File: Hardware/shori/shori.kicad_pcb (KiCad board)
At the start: 4 copper layers, 102.8 x 41 mm, 114 parts, among them U1 CS4272, U2 STM32H750VBTx, U3 NE5532, U4 NE5532, U5 TPS73733DCQR, U6 W25Q128JVS, U7 TLV9001IDCK, Y1 16MHz

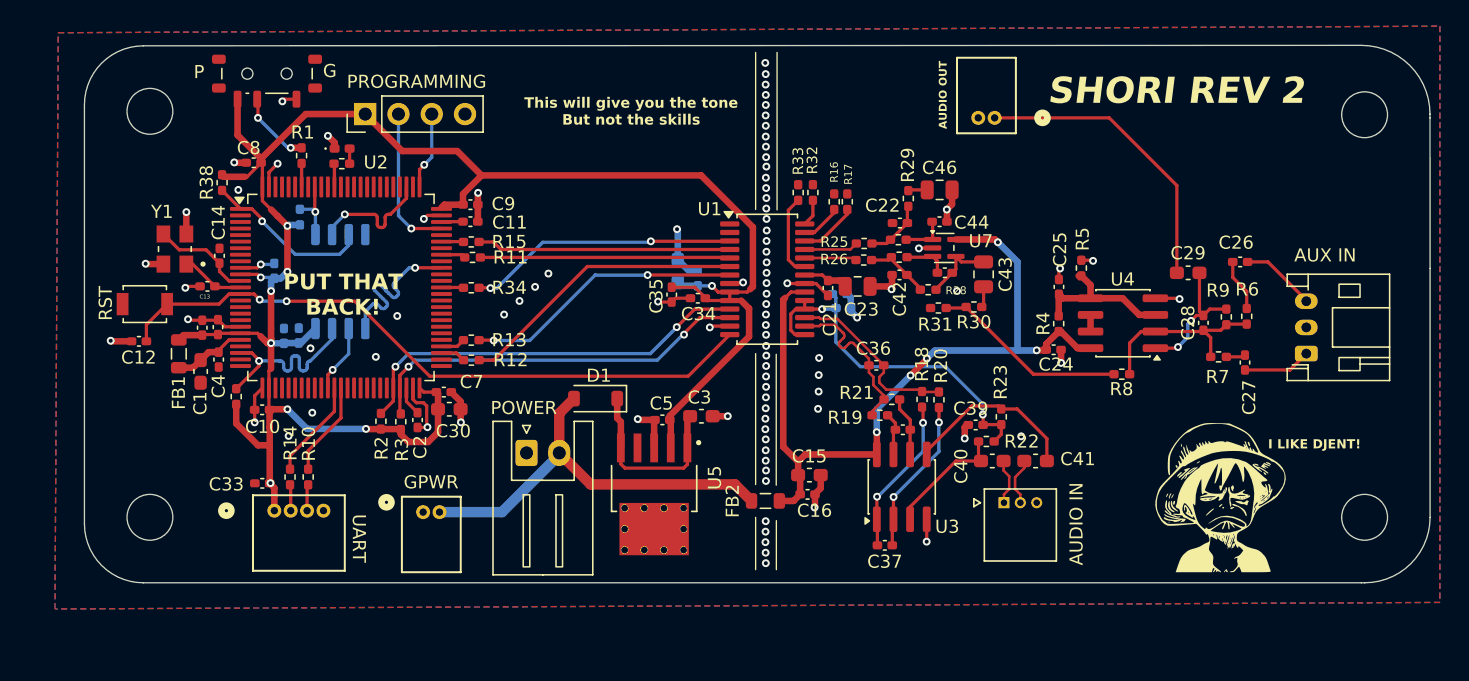
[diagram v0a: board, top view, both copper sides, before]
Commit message: Rev 3 changes: RC filters, Ideal diodes, electrical fixes, and their layout
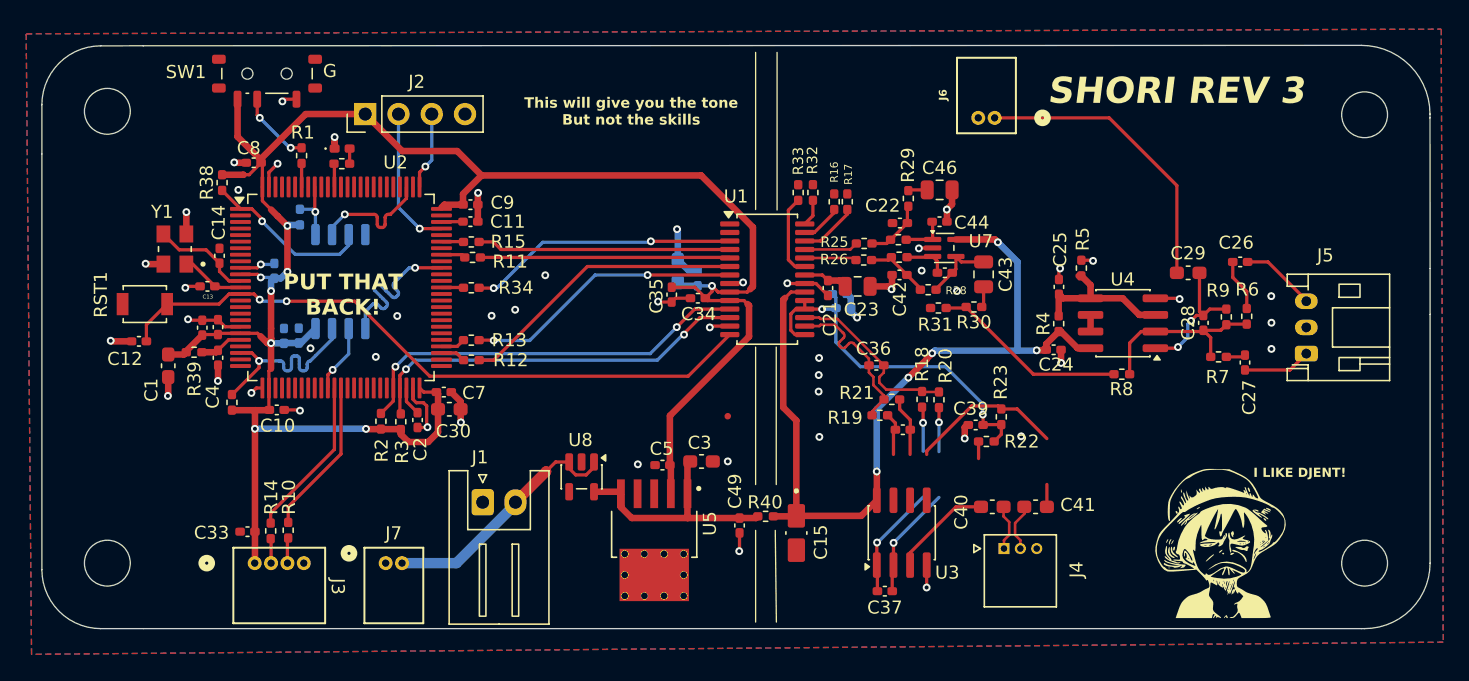
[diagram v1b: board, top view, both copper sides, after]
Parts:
- removed C16: 100nF, Capacitor_SMD:C_0402_1005Metric_Pad0.74x0.62mm_HandSolder
- removed D1: D_Schottky, Diode_SMD:D_SOD-123
- removed FB1, FB2: FerriteBead, Inductor_SMD:L_0805_2012Metric
- added C49: 100nF, Capacitor_SMD:C_0402_1005Metric_Pad0.74x0.62mm_HandSolder, F.Cu at (150.3, 127.6)
- added R39: 10Ω, Resistor_SMD:R_0402_1005Metric_Pad0.72x0.64mm_HandSolder, F.Cu at (108.6, 114.4)
- added R40: 10Ω, Resistor_SMD:R_0402_1005Metric_Pad0.72x0.64mm_HandSolder, F.Cu at (152.3, 126.9)
- added U8: MAX40200AUK, Package_TO_SOT_SMD:SOT-23-5, F.Cu at (138.2, 123.9)
- C1: value 4.7uf -> 100nF
- C15: value 10μF -> 100uF; footprint Capacitor_SMD:C_0603_1608Metric_Pad1.08x0.95mm_HandSolder -> MyFootprints:CAPPM3216X180N
- C4: value 100nF -> 10uF
- J4: renamed from AUDIO IN
- J5: renamed from AUX IN
- J6: renamed from AUDIO OUT
- moved J1 5.04 mm to (130.7, 125.8)
- moved J7 4.83 mm to (123.2, 130.5)
- moved H3 4.78 mm to (102.0, 130.5)
- moved C15 4.53 mm to (154.6, 128.2), turned to -90 degrees
- moved R14 4.37 mm to (114.5, 128.0)
- moved R10 4.34 mm to (115.8, 128.0)
- moved J3 4.28 mm to (113.2, 130.5)
- moved C33 3.86 mm to (112.7, 128.1)
- moved U5 3.50 mm to (143.8, 128.3)
- moved J4 3.50 mm to (170.5, 129.4)
- moved U3 3.50 mm to (162.7, 128.2)
- moved C37 3.50 mm to (161.4, 132.6)
- moved C40 3.50 mm to (169.6, 126.2)
- moved C41 3.50 mm to (172.9, 126.2)
- moved G*** 3.50 mm to (187.4, 127.5)
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- renumbered POWER to J1, PROGRAMMING to J2, UART to J3, GPWR to J7, RST to RST1, P to SW1
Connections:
- net Net-(D1-K) renamed /5V_PROTECTED
- C1 pad 1: +3.3VA -> +3.3V
- J2 pad 2: /SWCLK -> /SWDIO
- J2 pad 3: /SWDIO -> /SWCLK
- U2 pad 72: /SWCLK -> /SWDIO
- U2 pad 76: /SWDIO -> /SWCLK
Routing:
- net +5V: track 31.9 -> 19.4 mm
- net +3.3V: track 154.7 -> 162.9 mm, vias 9 -> 8
- net /5V_PROTECTED: track 14.2 -> 20.0 mm
- net GND: track 67.8 -> 62.3 mm, vias 95 -> 52
- net /SWCLK: track 11.4 -> 5.95 mm
- net +5VA: track 60.5 -> 65.9 mm
- net /SWDIO: track 5.95 -> 11.1 mm
- net /UART_RX_RES: track 7.60 -> 12.3 mm
- net /UART_TX_RES: track 7.24 -> 11.9 mm
- net +3.3VA: track 5.67 -> 3.34 mm
- net /QSPI_IO3: track 15.4 -> 16.0 mm
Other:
- board size 102.8 x 41 mm -> 106 x 44.5 mm
- board text added: "SHORI REV 3"
- board text removed: "SHORI REV 2"

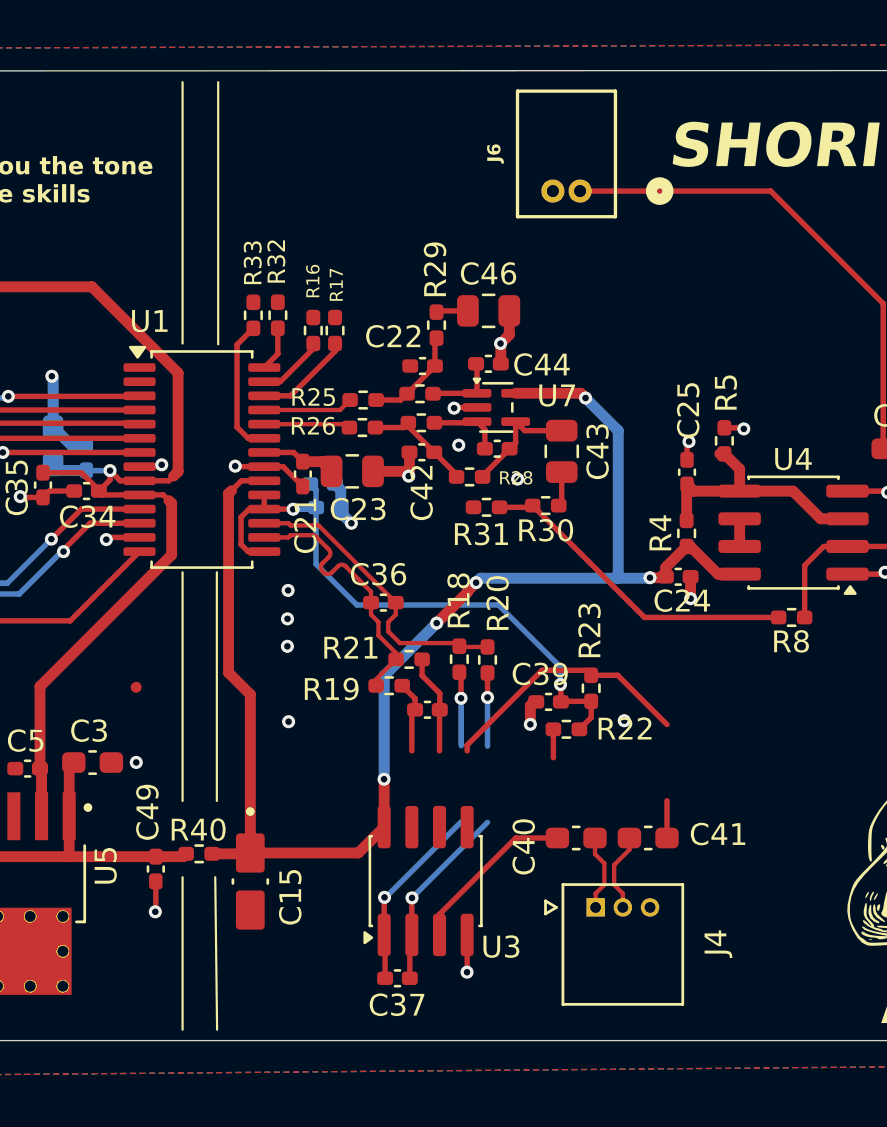
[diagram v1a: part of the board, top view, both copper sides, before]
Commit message: Power LED added on schems
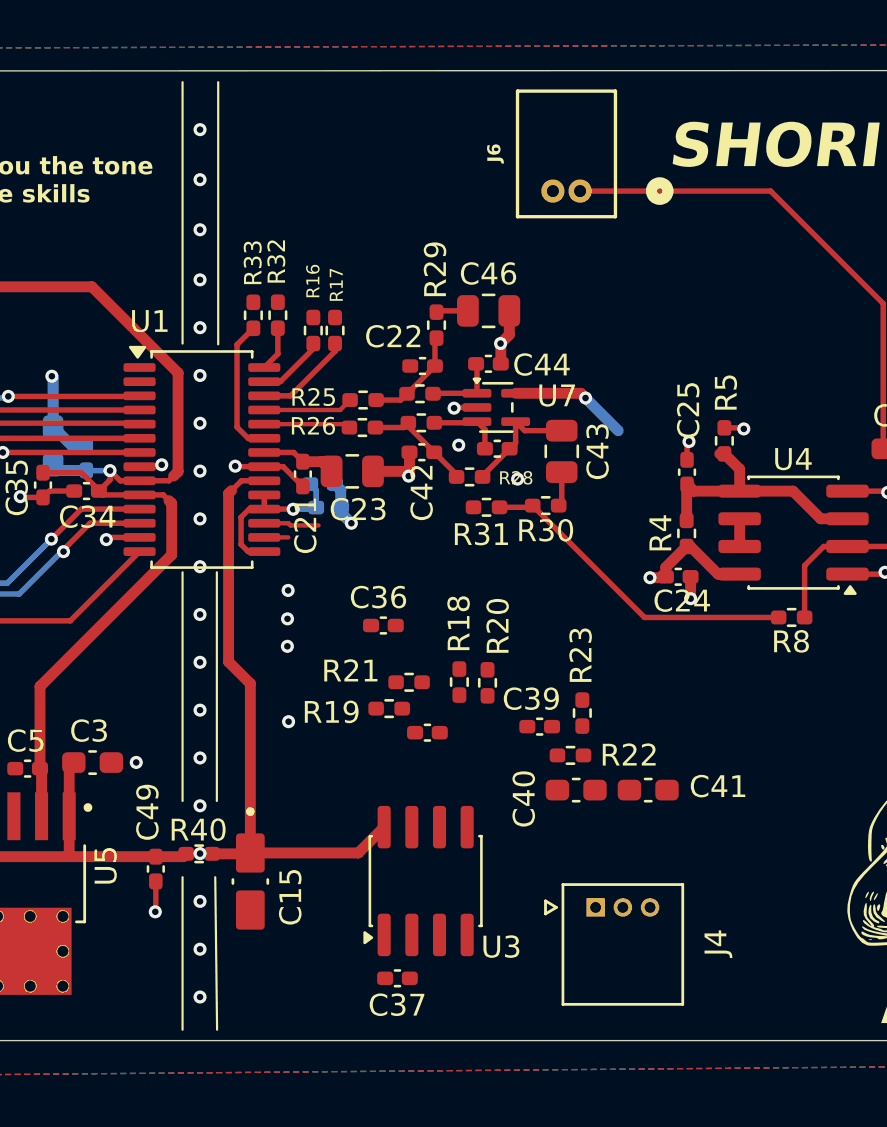
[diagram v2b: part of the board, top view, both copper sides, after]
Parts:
- moved C40 2.20 mm to (169.6, 124.0)
- moved C41 2.20 mm to (172.9, 124.0)
- moved R22 1.21 mm to (169.3, 122.4)
- moved C39 1.21 mm to (167.9, 121.1)
- moved R23 1.21 mm to (169.9, 120.5)
- moved R18 1.05 mm to (164.2, 119.0)
- moved R20 1.05 mm to (165.5, 119.1)
- moved C36 1.05 mm to (160.7, 116.4)
- moved C38 1.05 mm to (162.7, 121.4)
- moved R19 1.05 mm to (161.0, 120.3)
- moved R21 1.05 mm to (161.9, 119.0)
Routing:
- net +5VA: track 65.9 -> 38.1 mm, vias 5 -> 2
- net /VCOM: track 28.2 -> 7.92 mm, vias 2 -> 1
- net Net-(U3B-+): track 13.6 -> 0.00 mm
- net Net-(C37-Pad1): track 12.1 -> 0.00 mm, vias 2 -> 0
- net Net-(U3A--): track 12.0 -> 0.00 mm, vias 2 -> 0
- net /CODEC_AIN-: track 12.5 -> 1.11 mm
- net /CODEC_AIN+: track 13.9 -> 2.53 mm
- net Net-(U3A-+): track 9.38 -> 0.00 mm
- net Net-(U3B--): track 4.54 -> 0.00 mm
- net /AUDIO_IN-: track 3.64 -> 0.00 mm
- net /AUDIO_IN+: track 3.53 -> 0.00 mm
- net Net-(C38-Pad1): track 3.30 -> 0.00 mm
- net GND: track 62.3 -> 59.4 mm, vias 52 -> 68

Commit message: Rev 3 main changes completed!
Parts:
- added D1: LED, LED_SMD:LED_0603_1608Metric_Pad1.05x0.95mm_HandSolder, F.Cu at (138.7, 119.5)
- added D10: BAT54C, Package_TO_SOT_SMD:SOT-23, F.Cu at (188.9, 106.7)
- added D11: BAT54C, Package_TO_SOT_SMD:SOT-23, F.Cu at (189.4, 118.9)
- added D7: PRTR5V0U2X, Package_TO_SOT_SMD:SOT-143, F.Cu at (121.5, 124.4)
- added D8: BAT54C, Package_TO_SOT_SMD:SOT-23, F.Cu at (166.5, 127.3)
- added D9: BAT54C, Package_TO_SOT_SMD:SOT-23, F.Cu at (175.8, 126.5)
- added R41: 33Ω, Resistor_SMD:R_0402_1005Metric_Pad0.72x0.64mm_HandSolder, F.Cu at (142.4, 119.5)
- added R42: 100Ω, Resistor_SMD:R_0402_1005Metric_Pad0.72x0.64mm_HandSolder, F.Cu at (172.5, 126.4)
- added R43: 100Ω, Resistor_SMD:R_0402_1005Metric_Pad0.72x0.64mm_HandSolder, F.Cu at (169.9, 126.4)
- added R44: 100Ω, Resistor_SMD:R_0402_1005Metric_Pad0.72x0.64mm_HandSolder, F.Cu at (191.7, 106.8)
- added R45: 100Ω, Resistor_SMD:R_0402_1005Metric_Pad0.72x0.64mm_HandSolder, F.Cu at (192.3, 118.3)
- added TP1: TP_5V, TestPoint:TestPoint_Pad_D1.0mm, F.Cu at (149.0, 127.1)
- added TP2: TP_3V3, TestPoint:TestPoint_Pad_D1.0mm, F.Cu at (145.0, 119.5)
- added TP3: TP_3V3A, TestPoint:TestPoint_Pad_D1.0mm, F.Cu at (106.0, 116.5)
- added TP4: TP_5VA, TestPoint:TestPoint_Pad_D1.0mm, F.Cu at (156.0, 120.5)
- added TP5: TP_MCLK, TestPoint:TestPoint_Pad_D1.0mm, B.Cu at (138.0, 106.0)
- added TP6: TP_UARTTX, TestPoint:TestPoint_Pad_D1.0mm, F.Cu at (118.0, 124.0)
- moved C49 4.00 mm to (154.0, 129.1)
- moved R23 3.42 mm to (172.9, 122.0), turned to 180 degrees
- moved C38 3.35 mm to (160.7, 124.0)
- moved R19 2.71 mm to (160.1, 122.8), turned to 180 degrees
- moved R18 2.44 mm to (163.2, 121.3)
- moved R20 2.44 mm to (164.5, 121.3)
- moved R21 2.39 mm to (161.4, 121.4)
- moved C26 2.27 mm to (189.5, 109.5)
- moved C1 2.21 mm to (108.5, 116.6)
- moved U3 1.82 mm to (160.9, 128.5)
- moved C37 1.82 mm to (159.6, 133.0)
- moved C39 1.67 mm to (169.6, 121.0)
- moved G*** 1.43 mm to (185.9, 127.6)
- moved C15 1.36 mm to (156.0, 128.2)
- moved R22 1.15 mm to (170.4, 122.0)
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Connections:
- net Net-(SW1-B) renamed /BOOT0_R_TO_SW
- C1 pad 1: +3.3V -> +3.3VA
- C49 pad 1: /5V_PROTECTED -> +5VA
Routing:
- net +5VA: track 38.1 -> 107.1 mm, vias 2 -> 7
- net /VCOM: track 7.92 -> 27.6 mm, vias 1 -> 2
- net Net-(U3B-+): track 0.00 -> 13.8 mm, vias 0 -> 2
- net /CODEC_AIN+: track 2.53 -> 15.9 mm
- net Net-(U3A-+): track 0.00 -> 13.1 mm, vias 0 -> 2
- net Net-(C37-Pad1): track 0.00 -> 12.9 mm, vias 0 -> 2
- net Net-(U3A--): track 0.00 -> 12.9 mm, vias 0 -> 2
- net /CODEC_AIN-: track 1.11 -> 13.6 mm
- net +3.3V: track 162.9 -> 169.8 mm
- net /AUDIO_IN-: track 0.00 -> 6.32 mm
- net /AUDIO_IN+: track 0.00 -> 6.16 mm
- net /UART_RX_RES: track 12.3 -> 18.3 mm, vias 0 -> 2
- net Net-(U3B--): track 0.00 -> 5.00 mm
- net +3.3VA: track 3.34 -> 7.81 mm
- net Net-(C38-Pad1): track 0.00 -> 3.47 mm
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
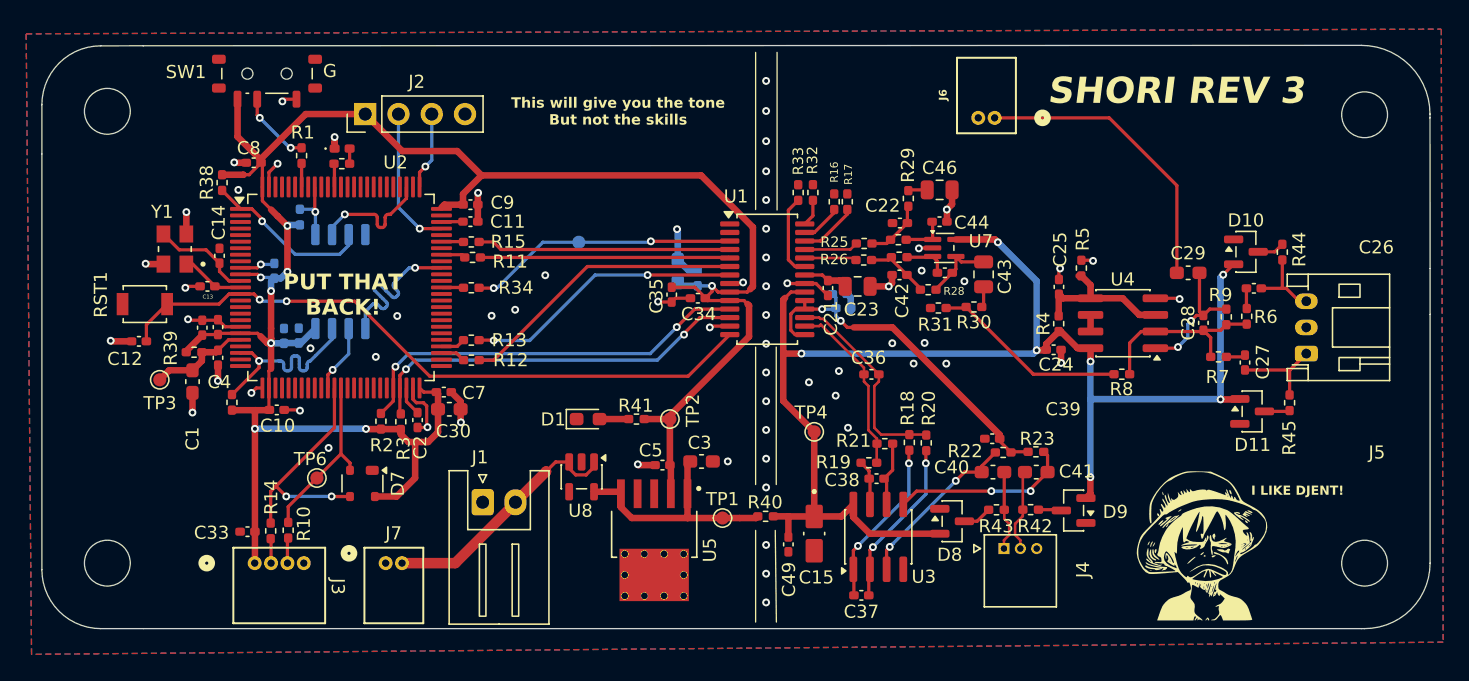
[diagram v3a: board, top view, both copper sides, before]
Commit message: removed gamen power conn and layout clean up
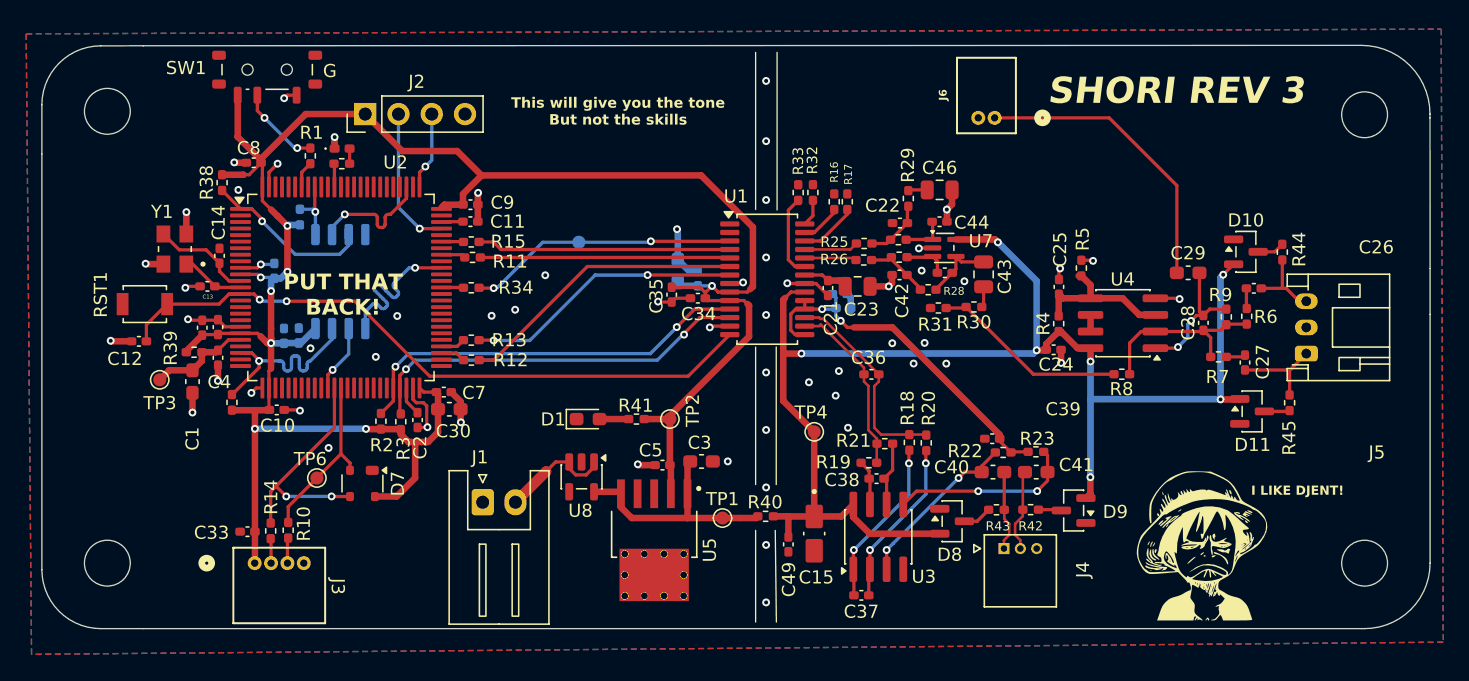
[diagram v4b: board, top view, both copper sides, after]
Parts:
- removed J7: 530480210, My footprints:CONN02_530480210_MOL
- moved G*** 11.9 mm to (176.0, 113.5), turned to 0 degrees
- moved G*** 4.74 mm to (149.0, 113.0), turned to 0 degrees
- moved R1 0.67 mm to (117.5, 99.4)
- moved SW1 0.31 mm to (114.2, 92.8)
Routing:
- net +5V: track 19.5 -> 8.97 mm
- net /BOOT0_R_TO_SW: track 5.65 -> 6.41 mm
- net GND: track 58.2 -> 58.1 mm, vias 67 -> 59

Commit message: Started Mae Schematics!!
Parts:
- AUDIO IN: renamed from J4
- AUDIO OUT: renamed from J6
- AUX IN: renamed from J5
- D1: footprint LED_SMD:LED_0603_1608Metric_Pad1.05x0.95mm_HandSolder -> LED_SMD:LED_0805_2012Metric_Pad1.15x1.40mm_HandSolder
- Y1: footprint MyFootprints:XTAL_ABM8-12.288MHZ-B2-T -> Crystal:Crystal_SMD_3225-4Pin_3.2x2.5mm
- moved Y1 0.05 mm to (107.2, 106.6), turned to 90 degrees
- renumbered J1 to POWER, J3 to UART
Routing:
- net /AUDIO_OUT: track 22.7 -> 18.8 mm
